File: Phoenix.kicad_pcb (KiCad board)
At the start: 2 copper layers, 83.2 x 37.6 mm, 88 parts, among them J1 Mini USB Female, J2 Battery Connector, J3 Pyro Connectors, Q1 2N7000, Q2 BSS84, Q3 IRFML8244TRPBF, Q4 IRFML8244TRPBF, Q5 IRFML8244TRPBF, Q6 IRFML8244TRPBF, U1 RP2040, U3 AMS1117-3.3, U4 I3G4250D, U5 MS5637-02BA03, U6 ADXL343, U8 Si4468/7, U9 L70B-M39, Y1 12MHz, Y2 30MHz

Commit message: Fixed power ports
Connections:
- C16 pad 1: +3.3V -> +3V3
- C17 pad 1: +3.3V -> +3V3
- C18 pad 1: +3.3V -> +3V3
- U4 pad 1: +3.3V -> +3V3
- U4 pad 15: +3.3V -> +3V3
- U4 pad 16: +3.3V -> +3V3
- U4 pad 5: +3.3V -> +3V3
- U5 pad 1: +3.3V -> +3V3
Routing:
- net +3V3: track 16.9 -> 24.8 mm
- net +3.3V: track 7.99 -> 0.00 mm
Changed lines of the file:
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@@
   (net 71 "Net-(Q1-Pad3)")
   (net 72 "Net-(Q2-Pad2)")
-  (net 73 "+3.3V")
+  (net 73 "Net-(F1-Pad2)")
   (net 74 "/Accelerometer/Gyro1")
   (net 75 "/Accelerometer/Gyro2")
@@
   (net 93 "Net-(JP1-Pad2)")
   (net 94 "Net-(R3-Pad1)")
-  (net 95 "Net-(J3-Pad10)")
   (footprint "Resistor_SMD:R_0603_1608Metric_Pad0.98x0.95mm_HandSolder" (layer "F.Cu")
     (at 105.156 38.79 90)
@@
       (net 9 "+BATT") (pintype "passive"))
     (pad "2" smd roundrect (at 0.7875 0 180) (size 0.875 0.95) (layers "F.Cu" "F.Paste" "F.Mask") (roundrect_rratio 0.25)
-      (net 95 "Net-(J3-Pad10)") (pintype "passive"))
+      (net 73 "Net-(F1-Pad2)") (pintype "passive"))
     (model "${KICAD6_3DMODEL_DIR}/Fuse.3dshapes/Fuse_0603_1608Metric.wrl"
       (offset (xyz 0 0 0))
@@
     (fp_line (start 0.8 -0.4) (end 0.8 0.4) (layer "F.Fab") (width 0.1))
     (pad "1" smd roundrect (at -0.775 0 270) (size 0.9 0.95) (layers "F.Cu" "F.Paste" "F.Mask") (roundrect_rratio 0.25)
-      (net 73 "+3.3V") (pintype "passive"))
+      (net 5 "+3V3") (pintype "passive"))
     (pad "2" smd roundrect (at 0.775 0 270) (size 0.9 0.95) (layers "F.Cu" "F.Paste" "F.Mask") (roundrect_rratio 0.25)
       (net 4 "GND") (pintype "passive"))
@@
     (fp_line (start -1.5 1.5) (end -1.5 -1.5) (layer "F.Fab") (width 0.2))
     (pad "1" smd rect (at -1 -1 90) (size 1 1) (layers "F.Cu" "F.Paste" "F.Mask")
-      (net 73 "+3.3V") (pinfunction "VDD") (pintype "input"))
+      (net 5 "+3V3") (pinfunction "VDD") (pintype "input"))
     (pad "2" smd rect (at -1 1 90) (size 1 1) (layers "F.Cu" "F.Paste" "F.Mask")
       (net 32 "/Accelerometer/SDA") (pinfunction "SDA") (pintype "bidirectional"))
@@
     (fp_line (start 2.075 -2.075) (end 2.075 2.075) (layer "F.Fab") (width 0.02))
     (pad "1" smd rect (at 1.775 -0.975 270) (size 0.4 0.3) (layers "F.Cu" "F.Paste" "F.Mask")
-      (net 73 "+3.3V") (pinfunction "Vdd_IO") (pintype "output"))
+      (net 5 "+3V3") (pinfunction "Vdd_IO") (pintype "output"))
     (pad "2" smd rect (at 1.775 -0.325 270) (size 0.4 0.3) (layers "F.Cu" "F.Paste" "F.Mask")
       (net 33 "/Accelerometer/SCL") (pinfunction "SCL/SPC") (pintype "input"))
@@
       (net 4 "GND") (pinfunction "SDO/SA0") (pintype "output"))
     (pad "5" smd rect (at 0.975 1.775 270) (size 0.3 0.4) (layers "F.Cu" "F.Paste" "F.Mask")
-      (net 73 "+3.3V") (pinfunction "CS") (pintype "input"))
+      (net 5 "+3V3") (pinfunction "CS") (pintype "input"))
     (pad "6" smd rect (at 0.325 1.775 270) (size 0.3 0.4) (layers "F.Cu" "F.Paste" "F.Mask")
       (net 75 "/Accelerometer/Gyro2") (pinfunction "DRDY/INT2") (pintype "output"))
@@
       (net 81 "Net-(C14-Pad2)") (pinfunction "PLLFILT") (pintype "input"))
     (pad "15" smd rect (at 0.325 -1.775 270) (size 0.3 0.4) (layers "F.Cu" "F.Paste" "F.Mask")
-      (net 73 "+3.3V") (pinfunction "RESERVED") (pintype "free"))
+      (net 5 "+3V3") (pinfunction "RESERVED") (pintype "free"))
     (pad "16" smd rect (at 0.975 -1.775 270) (size 0.3 0.4) (layers "F.Cu" "F.Paste" "F.Mask")
-      (net 73 "+3.3V") (pinfunction "VDD") (pintype "output"))
+      (net 5 "+3V3") (pinfunction "VDD") (pintype "output"))
   )
   (footprint "Resistor_SMD:R_Array_Convex_4x0603" (layer "F.Cu")
@@
     (fp_line (start -0.8 -0.4) (end 0.8 -0.4) (layer "F.Fab") (width 0.1))
     (pad "1" smd roundrect (at -0.775 0 270) (size 0.9 0.95) (layers "F.Cu" "F.Paste" "F.Mask") (roundrect_rratio 0.25)
-      (net 73 "+3.3V") (pintype "passive"))
+      (net 5 "+3V3") (pintype "passive"))
     (pad "2" smd roundrect (at 0.775 0 270) (size 0.9 0.95) (layers "F.Cu" "F.Paste" "F.Mask") (roundrect_rratio 0.25)
       (net 4 "GND") (pintype "passive"))
@@
     (fp_line (start 0.8 -0.4) (end 0.8 0.4) (layer "F.Fab") (width 0.1))
     (pad "1" smd roundrect (at -0.775 0 270) (size 0.9 0.95) (layers "F.Cu" "F.Paste" "F.Mask") (roundrect_rratio 0.25)
-      (net 73 "+3.3V") (pintype "passive"))
+      (net 5 "+3V3") (pintype "passive"))
     (pad "2" smd roundrect (at 0.775 0 270) (size 0.9 0.95) (layers "F.Cu" "F.Paste" "F.Mask") (roundrect_rratio 0.25)
       (net 4 "GND") (pintype "passive"))
@@
       (net 41 "/GPIO & Pyro/Pyro Power") (pinfunction "Pin_9") (pintype "passive"))
     (pad "10" thru_hole circle (at 11.43 0 90) (size 1.524 1.524) (drill 0.762) (layers *.Cu *.Mask)
-      (net 95 "Net-(J3-Pad10)") (pinfunction "Pin_10") (pintype "passive"))
+      (net 73 "Net-(F1-Pad2)") (pinfunction "Pin_10") (pintype "passive"))
   )
   (footprint "Button_Switch_SMD:SW_SPST_B3U-1000P" (layer "F.Cu")
@@
   (via (at 123.796284 40.287944) (size 0.8) (drill 0.4) (layers "F.Cu" "B.Cu") (free) (net 4))
   (via (at 105.804 55.5305) (size 0.8) (drill 0.4) (layers "F.Cu" "B.Cu") (free) (net 4))
+  (segment (start 126.718 42.2815) (end 126.746 42.3095) (width 0.2) (layer "F.Cu") (net 5))
+  (segment (start 124.64 42.2815) (end 126.718 42.2815) (width 0.2) (layer "F.Cu") (net 5))
+  (segment (start 129.970948 42.323293) (end 131.349207 42.323293) (width 0.2) (layer "F.Cu") (net 5))
   (segment (start 104.254 55.5305) (end 104.267 55.5305) (width 0.2) (layer "F.Cu") (net 5))
+  (segment (start 126.746 42.3095) (end 129.823 42.3095) (width 0.2) (layer "F.Cu") (net 5))
   (segment (start 126.537926 36.031426) (end 126.733 36.2265) (width 0.2) (layer "F.Cu") (net 5))
+  (segment (start 131.349207 42.323293) (end 132.35 41.3225) (width 0.2) (layer "F.Cu") (net 5))
   (via (at 126.733 36.2265) (size 0.8) (drill 0.4) (layers "F.Cu" "B.Cu") (net 5))
   (via (at 130.404 29.6225) (size 0.8) (drill 0.4) (layers "F.Cu" "B.Cu") (net 5))
@@
   (segment (start 75.18329 34.2225) (end 74.58329 33.6225) (width 0.2) (layer "F.Cu") (net 72))
   (segment (start 81.787 34.2225) (end 75.18329 34.2225) (width 0.2) (layer "F.Cu") (net 72))
-  (segment (start 126.718 42.2815) (end 126.746 42.3095) (width 0.2) (layer "F.Cu") (net 73))
-  (segment (start 124.64 42.2815) (end 126.718 42.2815) (width 0.2) (layer "F.Cu") (net 73))
-  (segment (start 129.970948 42.323293) (end 131.349207 42.323293) (width 0.2) (layer "F.Cu") (net 73))
-  (segment (start 126.746 42.3095) (end 129.823 42.3095) (width 0.2) (layer "F.Cu") (net 73))
-  (segment (start 131.349207 42.323293) (end 132.35 41.3225) (width 0.2) (layer "F.Cu") (net 73))
+  (segment (start 70.8405 36.9885) (end 66.294 36.9885) (width 0.5) (layer "F.Cu") (net 73))
   (segment (start 110.547696 41.003776) (end 110.547696 37.729756) (width 0.2) (layer "F.Cu") (net 74))
   (segment (start 110.547696 37.729756) (end 117.538256 37.729756) (width 0.2) (layer "F.Cu") (net 74))
@@
   (segment (start 101.6 44.305787) (end 102.301522 45.007309) (width 0.2) (layer "F.Cu") (net 94))
   (segment (start 101.6 41.6875) (end 101.6 44.305787) (width 0.2) (layer "F.Cu") (net 94))
-  (segment (start 70.8405 36.9885) (end 66.294 36.9885) (width 0.5) (layer "F.Cu") (net 95))
   (zone (net 4) (net_name "GND") (layers F&B.Cu) (hatch edge 0.508)
     (connect_pads (clearance 0.2))

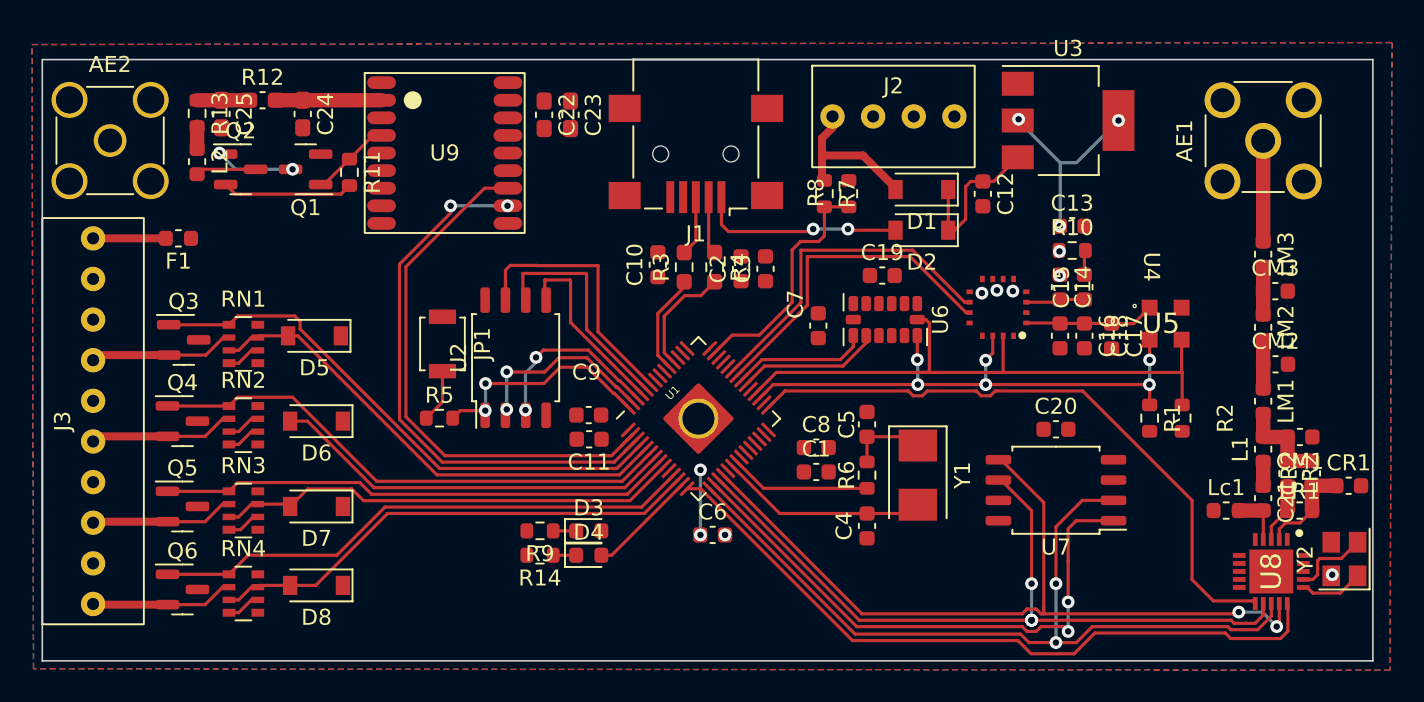
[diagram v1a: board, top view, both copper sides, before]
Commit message: Routed power traces
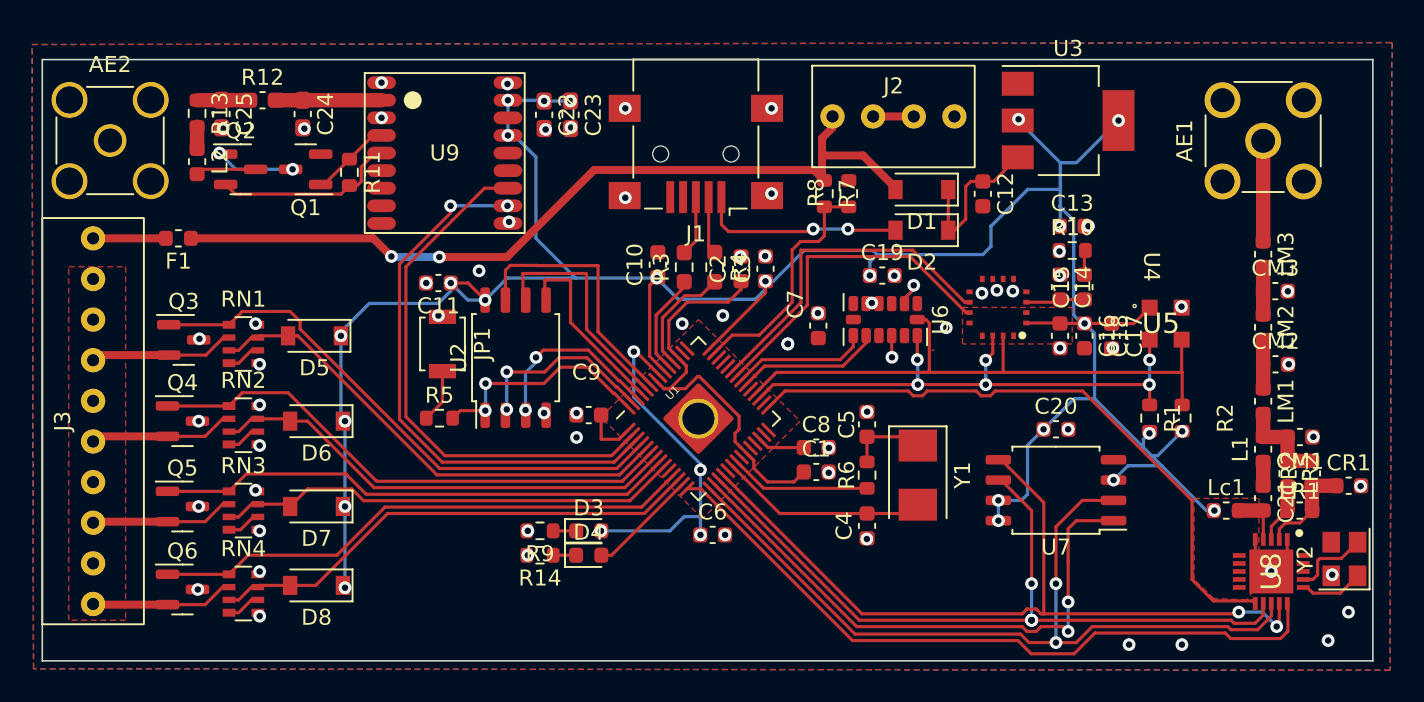
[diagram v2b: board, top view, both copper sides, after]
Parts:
- moved C11 13.6 mm to (87.9, 39.8)
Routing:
- net +3V3: track 24.8 -> 192.9 mm, vias 5 -> 28
- net +BATT: track 9.92 -> 52.5 mm, vias 0 -> 2
- net +1V1: track 0.00 -> 25.0 mm
- net GND: track 0.00 -> 7.58 mm, vias 7 -> 69
- net Net-(Q2-Pad2): track 8.21 -> 11.6 mm
- net /Power Supply/VBat in: track 0.00 -> 2.54 mm
- net /GPIO & Pyro/Cont2: track 27.5 -> 29.6 mm
- added copper zone on F.Cu, net +3V3
- added copper zone on F.Cu, net /GPIO & Pyro/Pyro Power

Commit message: Fixed some errors
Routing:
- net GND: vias 69 -> 67
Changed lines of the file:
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@@
   (via (at 76.708 60.6105) (size 0.8) (drill 0.4) (layers "F.Cu" "B.Cu") (net 4))
   (via (at 96.176299 30.057312) (size 0.8) (drill 0.4) (layers "F.Cu" "B.Cu") (net 4))
+  (via (at 119.634 44.4815) (size 0.8) (drill 0.4) (layers "F.Cu" "B.Cu") (free) (net 4))
   (via (at 126.711526 37.80667) (size 0.8) (drill 0.4) (layers "F.Cu" "B.Cu") (net 4))
   (via (at 72.898 53.7525) (size 0.8) (drill 0.4) (layers "F.Cu" "B.Cu") (net 4))
@@
   (via (at 108.712 34.1945) (size 0.8) (drill 0.4) (layers "F.Cu" "B.Cu") (net 4))
   (via (at 92.202 27.3365) (size 0.8) (drill 0.4) (layers "F.Cu" "B.Cu") (net 4))
-  (via (at 119.634 42.5765) (size 0.8) (drill 0.4) (layers "F.Cu" "B.Cu") (free) (net 4))
   (via (at 90.424 39.0205) (size 0.8) (drill 0.4) (layers "F.Cu" "B.Cu") (free) (net 4))
   (via (at 112.295713 50.094188) (size 0.8) (drill 0.4) (layers "F.Cu" "B.Cu") (net 4))
@@
   (via (at 96.52 49.4345) (size 0.8) (drill 0.4) (layers "F.Cu" "B.Cu") (net 4))
   (via (at 143.764 58.0195) (size 0.8) (drill 0.4) (layers "F.Cu" "B.Cu") (net 4))
-  (via (at 109.728 43.5925) (size 0.8) (drill 0.4) (layers "F.Cu" "B.Cu") (free) (net 4))
   (via (at 114.668041 55.786076) (size 0.8) (drill 0.4) (layers "F.Cu" "B.Cu") (net 4))
   (via (at 76.708 47.4025) (size 0.8) (drill 0.4) (layers "F.Cu" "B.Cu") (net 4))
@@
   (via (at 93.472 56.8005) (size 0.8) (drill 0.4) (layers "F.Cu" "B.Cu") (net 4))
   (via (at 79.502 30.1305) (size 0.8) (drill 0.4) (layers "F.Cu" "B.Cu") (net 4))
-  (via (at 109.728 43.5925) (size 0.8) (drill 0.4) (layers "F.Cu" "B.Cu") (free) (net 4))
   (via (at 76.708 44.8625) (size 0.8) (drill 0.4) (layers "F.Cu" "B.Cu") (net 4))
   (via (at 74.422 30.1305) (size 0.8) (drill 0.4) (layers "F.Cu" "B.Cu") (net 4))
@@
   (segment (start 101.492 41.7955) (end 101.492 44.197787) (width 0.2) (layer "F.Cu") (net 94))
   (segment (start 103.251 40.0365) (end 101.492 41.7955) (width 0.2) (layer "F.Cu") (net 94))
+  (zone (net 5) (net_name "+3V3") (layer "F.Cu") (hatch edge 0.508)
+    (priority 1)
+    (connect_pads yes (clearance 0.2))
+    (min_thickness 0.2) (filled_areas_thickness no)
+    (fill yes (thermal_gap 0.508) (thermal_bridge_width 0.508))
+    (polygon
+      (pts
+        (xy 120.396 43.8465)
+        (xy 110.49 43.8465)
+        (xy 110.49 37.8775)
+        (xy 120.396 37.8775)
+      )
+    )
+  )
   (zone (net 41) (net_name "/GPIO & Pyro/Pyro Power") (layer "F.Cu") (hatch edge 0.508)
     (priority 1)
